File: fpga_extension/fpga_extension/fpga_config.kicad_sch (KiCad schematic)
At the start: 12 parts

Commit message: refactored mainboard schematic
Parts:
- removed C? (x4): 0.1u, Capacitor_SMD:C_0201_0603Metric_Pad0.64x0.40mm_HandSolder, symbol Device:C
- removed C? (x2): 10u, Capacitor_SMD:C_0603_1608Metric_Pad1.08x0.95mm_HandSolder, symbol Device:C
- removed R? (x3): 4.7k, Resistor_SMD:R_0603_1608Metric_Pad0.98x0.95mm_HandSolder, symbol Device:R
- removed U? (x3): LFE5U-25F-6BG381x, Package_BGA:Lattice_caBGA-381_17.0x17.0mm_Layout20x20_P0.8mm_Ball0.4mm_Pad0.4mm_NSMD, symbol fpga_extension_library:LFE5U-25F-6BG381x
- added C13, C15, C16, C18, C19: 0.1u, Capacitor_SMD:C_0201_0603Metric_Pad0.64x0.40mm_HandSolder, symbol Device:C
- added C14, C17: 10u, Capacitor_SMD:C_0603_1608Metric_Pad1.08x0.95mm_HandSolder, symbol Device:C
- added C26, C27: 0.47u, Capacitor_SMD:C_0201_0603Metric_Pad0.64x0.40mm_HandSolder, symbol Device:C
- added R1, R2, R3, R4, R5, R? (x2): 1k, symbol Device:R
- added R?: 20R, symbol Device:R
- added U2: ~, Package_TO_SOT_SMD:SOT-23-5, symbol fpga_extension_library:SiT2001B
- added U6: LFE5UM-85F-6BG381x, Package_BGA:Lattice_caBGA-381_17.0x17.0mm_Layout20x20_P0.8mm_Ball0.4mm_Pad0.4mm_NSMD, symbol FPGA_Lattice:LFE5UM-85F-6BG381x
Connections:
- net GND: now also C13.2, C14.2, C15.2, C16.2, C17.2, C18.2, C19.2, C26.2, C27.2, R3.1, R4.1, R5.1, U2.1 (GND)
- new net: R?.2, U2.3 (OE)
- new net: R2.1, R3.2, U6.R4 (CFG_2)
- new net: R1.1, R4.2, U6.T4 (CFG_1)
- new net: R5.2, R?.1, U6.U4 (CFG_0)
- new net: R?.1, U2.5 (OUT)
- new net +3V3: C13.1, C14.1, C15.1, C16.1, C17.1, C18.1, C19.1, C26.1, C27.1, R1.2, R2.2, R?.1, R?.2, U2.4 (VDD), U6.F11 (VCCIO1), U6.F12 (VCCIO1), U6.P10 (VCCIO8), U6.P9 (VCCIO8)
- new net BUS.CLK: U6.D11 (PT69A), U6.U3 (CCLK)
- new net BUS.CS#0: U6.T2 (PB13A)
- new net BUS.CS#1: U6.R2 (PB15A)
- new net BUS.INT: U6.U2 (PB13B)
- new net BUS.IO0: U6.R1 (PB4A)
- new net BUS.IO1: U6.T1 (PB4B)
- new net BUS.IO2: U6.U1 (PB6A)
- new net BUS.IO3: U6.V1 (PB6B)
- new net BUS.IO4: U6.W1 (PB9A)
- new net BUS.IO5: U6.Y2 (PB9B)
- new net BUS.IO6: U6.V2 (PB11A)
- new net BUS.IO7: U6.W2 (PB11B)
- new net BUS.RE#: U6.W3 (~{PROGRAM})
- new net BUS.RWDS: U6.D12 (PT74A)
- new net JTAG.TCK: U6.T5 (TCK)
- new net JTAG.TDI: U6.R5 (TDI)
- new net JTAG.TDO: U6.V4 (TDO)
- new net JTAG.TMS: U6.U5 (TMS)
- new net REF_CLK: R?.2, U6.B12 (PT71A)
- new net SDMMC.CLK: U6.B13 (PT78A)
- new net SDMMC.CMD: U6.A13 (PT76B)
- new net SDMMC.DAT0: U6.B15 (PT105A)
- new net SDMMC.DAT1: U6.A12 (PT76A)
- new net SDMMC.DAT2: U6.D14 (PT85A)
- new net SDMMC.DAT3: U6.A14 (PT83A)
- no-connect marks 40 -> 28

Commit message: prepared first versions of PCBs
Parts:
- removed C13, C15, C16, C18, C19: 0.1u, Capacitor_SMD:C_0201_0603Metric_Pad0.64x0.40mm_HandSolder, symbol Device:C
- removed C14, C17: 10u, Capacitor_SMD:C_0603_1608Metric_Pad1.08x0.95mm_HandSolder, symbol Device:C
- removed C26, C27: 0.47u, Capacitor_SMD:C_0201_0603Metric_Pad0.64x0.40mm_HandSolder, symbol Device:C
- removed R? (x2): 1k, symbol Device:R
- removed R?: 20R, symbol Device:R
- removed U2: ~, Package_TO_SOT_SMD:SOT-23-5, symbol fpga_extension_library:SiT2001B
- removed U6: LFE5UM-85F-6BG381x, Package_BGA:Lattice_caBGA-381_17.0x17.0mm_Layout20x20_P0.8mm_Ball0.4mm_Pad0.4mm_NSMD, symbol FPGA_Lattice:LFE5UM-85F-6BG381x
- added C2: 100n, Capacitor_SMD:C_0402_1005Metric_Pad0.74x0.62mm_HandSolder, symbol Device:C
- added R10, R12, R13, R14, R6, R8: 4.7k, Resistor_SMD:R_0402_1005Metric_Pad0.72x0.64mm_HandSolder, symbol Device:R
- added R11, R15, R7: DNF, Resistor_SMD:R_0402_1005Metric_Pad0.72x0.64mm_HandSolder, symbol Device:R
- added R9: 1k, Resistor_SMD:R_0402_1005Metric_Pad0.72x0.64mm_HandSolder, symbol Device:R
- added U1: LFE5UM-85F-7BG381x, Package_BGA:Lattice_caBGA-381_17.0x17.0mm_Layout20x20_P0.8mm_Ball0.4mm_Pad0.4mm_NSMD, symbol FPGA_Lattice:LFE5UM-85F-7BG381x
- added U2: W25Q128JVS, Package_SO:SOIC-8_5.23x5.23mm_P1.27mm, symbol Memory_Flash:W25Q128JVS
- R1, R2, R3, R4, R5: value 1k -> 4.7k; footprint (none) -> Resistor_SMD:R_0402_1005Metric_Pad0.72x0.64mm_HandSolder
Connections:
- net +3V3: now also R2.1, R3.1, R4.1, R5.1, C2.1, R10.1, R12.1, R13.1, R14.1, R6.1, R8.1, R9.1, U1.P10 (VCCIO8), U1.P9 (VCCIO8), U2.8 (VCC); no longer R1.2, R2.2
- net GND: now also R1.2, C2.2, R11.2, R15.2, R7.2, U2.4 (GND); no longer R3.1, R4.1, R5.1
- net JTAG.TCK: now also R1.1, U1.T5 (TCK)
- net JTAG.TDI: now also R3.2, U1.R5 (TDI)
- net JTAG.TDO: now also R4.2, U1.V4 (TDO)
- net JTAG.TMS: now also R5.2, U1.U5 (TMS)
- new net CFG.CFG0: R13.2, R15.1, U1.U4 (CFG_0)
- new net CFG.CFG1: R10.2, R11.1, U1.T4 (CFG_1)
- new net CFG.CFG2: R6.2, R7.1, U1.R4 (CFG_2)
- new net CFG.CLK: R9.2, U1.U3 (CCLK), U2.6 (CLK)
- new net CFG.CSS: R2.2, U1.R3 (PB15B), U2.1 (~{CS})
- new net CFG.DONE: R8.2, U1.Y3 (DONE)
- new net CFG.INIT#: R12.2, U1.V3 (~{INIT})
- new net CFG.IO2: U1.Y2 (PB9B), U2.3 (IO2)
- new net CFG.IO3: U1.W1 (PB9A), U2.7 (IO3)
- new net CFG.MISO: U1.V2 (PB11A), U2.2 (DO(IO1))
- new net CFG.MOSI: U1.W2 (PB11B), U2.5 (DI(IO0))
- new net CFG.PROGRAM#: R14.2, U1.W3 (~{PROGRAM})
- no-connect marks 28 -> 8
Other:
- note added: "Select correct configuration on PCB"

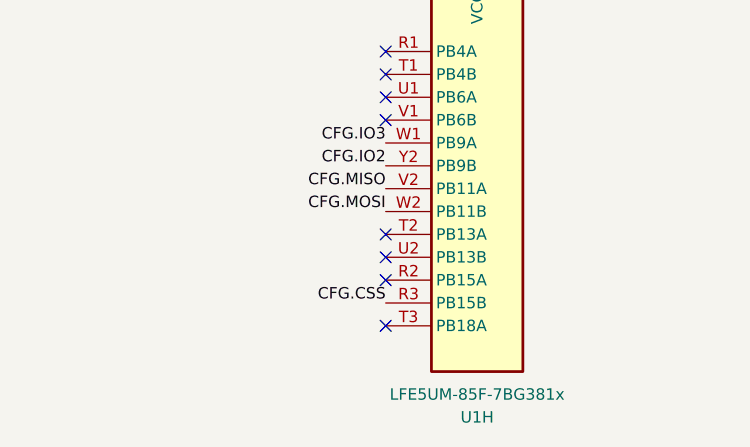
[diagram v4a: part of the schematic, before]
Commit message: fixed trace to flash memory
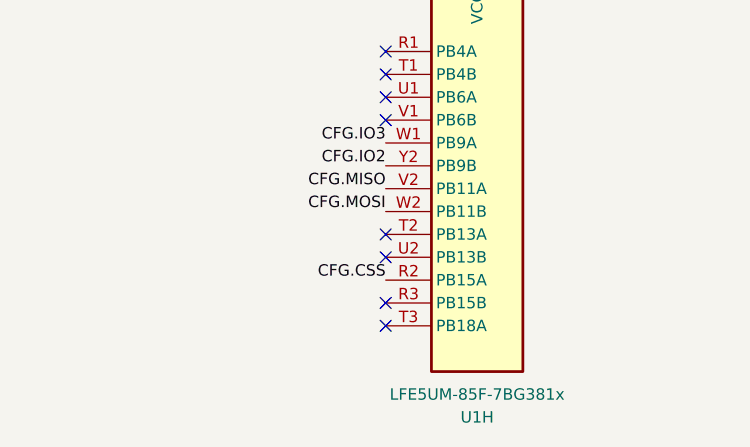
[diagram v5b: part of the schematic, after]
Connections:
- net CFG.CSS: now also U1.R2 (PB15A); no longer U1.R3 (PB15B)
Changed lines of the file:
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@@
+	)
+	(no_connect
+		(at 77.47 149.86)
 	)
 	(no_connect
@@
 	(no_connect
 		(at 77.47 144.78)
-	)
-	(no_connect
-		(at 77.47 147.32)
 	)
 	(bus_entry
@@
 		)
 	)
+	(label "CFG.CSS"
+		(at 77.47 147.32 180)
+		(fields_autoplaced yes)
+		(effects
+			(font
+				(size 1.27 1.27)
+			)
+			(justify right bottom)
+		)
+	)
 	(label "CFG.DONE"
 		(at 100.33 29.21 0)
@@
 		)
 	)
-	(label "CFG.CSS"
-		(at 77.47 149.86 180)
-		(fields_autoplaced yes)
-		(effects
-			(font
-				(size 1.27 1.27)
-			)
-			(justify right bottom)
-		)
-	)
